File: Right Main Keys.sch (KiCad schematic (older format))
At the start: 6 parts

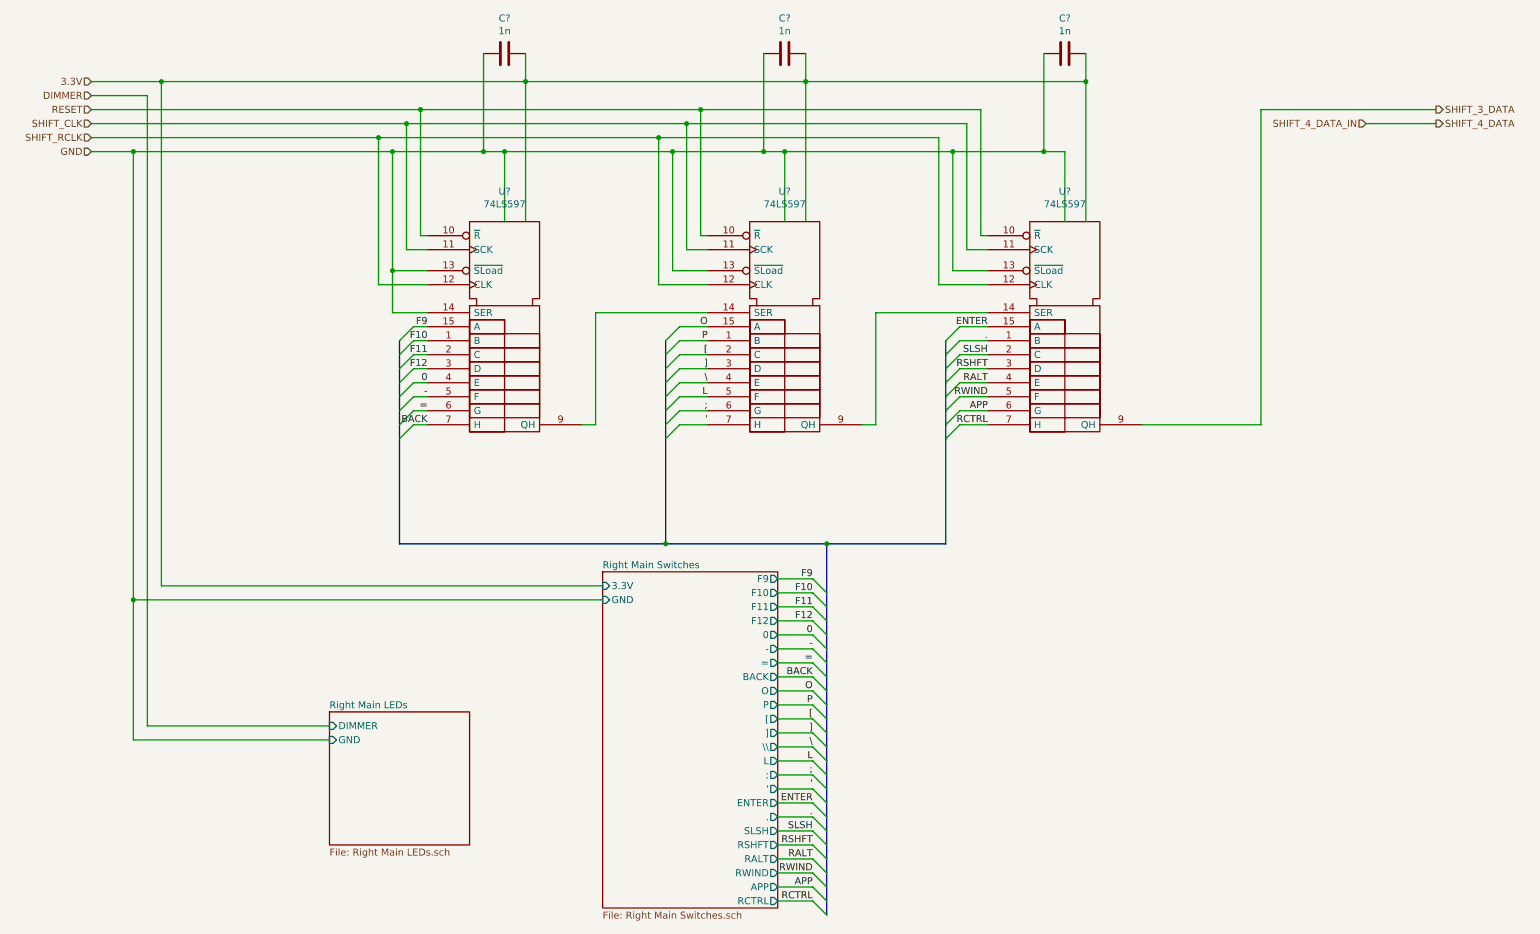
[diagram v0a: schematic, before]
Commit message: Fixed PISO Shift Register Wiring
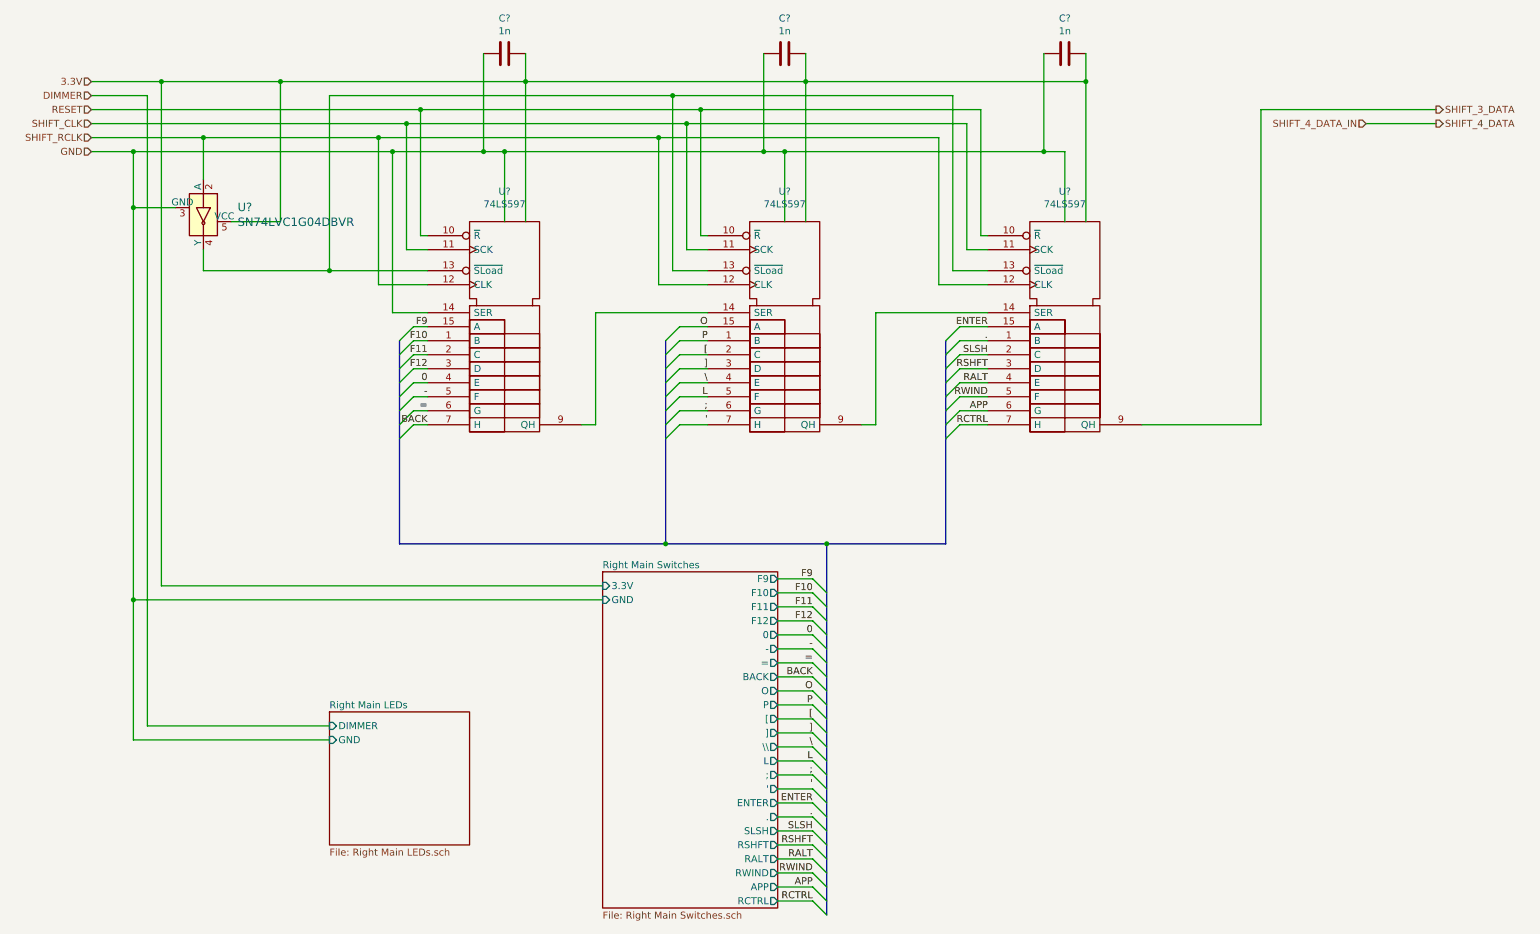
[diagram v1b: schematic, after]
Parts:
- added U?: SN74LVC1G04DBVR, digikey-footprints:SOT-753, symbol dk_Logic-Gates-and-Inverters:SN74LVC1G04DBVR
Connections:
- net GND: now also U?.3 (GND); no longer U?.13 (~SLoad), U?.13 (~SLoad), U?.13 (~SLoad)
- net SHIFT_RCLK: now also U?.2 (A)
- net VCC: now also U?.5 (VCC)
- new net: U?.13 (~SLoad), U?.13 (~SLoad), U?.13 (~SLoad), U?.4 (Y)
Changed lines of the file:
@@
 	3950 1600 3950 2100
-Wire Wire Line
-	3950 1600 5150 1600
 Wire Wire Line
 	5950 1600 5950 2100
@@
 Connection ~ 8100 1100
 Wire Wire Line
-	5950 1600 7150 1600
-Wire Wire Line
 	3350 1300 3350 2200
 Wire Wire Line
@@
 	7250 2300 7400 2300
 Connection ~ 5250 1400
-Wire Wire Line
-	3400 2450 3150 2450
-Wire Wire Line
-	3150 2450 3150 1600
 Connection ~ 3150 1600
 Wire Wire Line
@@
 Connection ~ 3050 1500
 Wire Wire Line
-	5400 2450 5150 2450
-Wire Wire Line
-	5150 2450 5150 1600
-Connection ~ 5150 1600
-Wire Wire Line
-	5150 1600 5800 1600
-Wire Wire Line
-	7400 2450 7150 2450
-Wire Wire Line
-	7150 2450 7150 1600
-Connection ~ 7150 1600
-Wire Wire Line
-	7150 1600 7800 1600
-Wire Wire Line
 	3050 1500 5050 1500
 Wire Wire Line
@@
 	5050 1500 7050 1500
 Wire Wire Line
-	3150 2450 3150 2750
-Wire Wire Line
 	3150 2750 3400 2750
-Connection ~ 3150 2450
 $Comp
 L Device:C C?
@@
 	9350 1300 9350 3550
 Wire Wire Line
-	1500 1100 4100 1100
+	1500 1100 2350 1100
 Connection ~ 1500 1100
 Wire Wire Line
@@
 	1000 1400 3250 1400
 Wire Wire Line
-	1000 1500 3050 1500
+	1000 1500 1800 1500
 Wire Wire Line
 	1300 1600 3150 1600
@@
 	8500 3550 9350 3550
 Wire Wire Line
-	1300 1600 1300 4800
+	1300 1600 1300 2000
 Wire Wire Line
 	4650 4800 1300 4800
@@
 	7100 4400 6250 4400
 Connection ~ 6250 4400
-Wire Bus Line
-	3200 2950 3200 4400
-Wire Bus Line
-	5100 2950 5100 4400
-Wire Bus Line
-	7100 2950 7100 4400
-Wire Bus Line
-	6250 4400 6250 7050
 $Sheet
 S 2700 5600 1000 950
@@
 F3 "GND" I L 2700 5800 50
 $EndSheet
+Wire Wire Line
+	3150 1600 3150 2750
+Wire Wire Line
+	3950 1600 5800 1600
+Wire Wire Line
+	5950 1600 7800 1600
+$Comp
+L dk_Logic-Gates-and-Inverters:SN74LVC1G04DBVR U?
+U 1 1 5EE3072F
+P 1800 2100
+AR Path="/5E8C755A/5EE3072F" Ref="U?"  Part="1"
+AR Path="/5E8C77AE/5EE3072F" Ref="U?"  Part="1"
+F 0 "U?" V 1697 2344 60  0000 L CNN
+F 1 "SN74LVC1G04DBVR" V 1803 2344 60  0000 L CNN
+F 2 "digikey-footprints:SOT-753" H 2000 2300 60  0001 L CNN
+F 3 "http://www.ti.com/general/docs/suppproductinfo.tsp?distId=10&gotoUrl=http%3A%2F%2Fwww.ti.com%2Flit%2Fgpn%2Fsn74lvc1g04" H 2000 2400 60  0001 L CNN
+F 4 "296-11599-1-ND" H 2000 2500 60  0001 L CNN "Digi-Key_PN"
+F 5 "SN74LVC1G04DBVR" H 2000 2600 60  0001 L CNN "MPN"
+F 6 "Integrated Circuits (ICs)" H 2000 2700 60  0001 L CNN "Category"
+F 7 "Logic - Gates and Inverters" H 2000 2800 60  0001 L CNN "Family"
+F 8 "http://www.ti.com/general/docs/suppproductinfo.tsp?distId=10&gotoUrl=http%3A%2F%2Fwww.ti.com%2Flit%2Fgpn%2Fsn74lvc1g04" H 2000 2900 60  0001 L CNN "DK_Datasheet_Link"
+F 9 "/product-detail/en/texas-instruments/SN74LVC1G04DBVR/296-11599-1-ND/385738" H 2000 3000 60  0001 L CNN "DK_Detail_Page"
+F 10 "IC INVERTER 1CH 1-INP SOT23-5" H 2000 3100 60  0001 L CNN "Description"
+F 11 "Texas Instruments" H 2000 3200 60  0001 L CNN "Manufacturer"
+F 12 "Active" H 2000 3300 60  0001 L CNN "Status"
+	1    1800 2100
+	0    1    1    0
+$EndComp
+Wire Wire Line
+	1800 1800 1800 1500
+Connection ~ 1800 1500
+Wire Wire Line
+	1800 1500 3050 1500
+Wire Wire Line
+	1600 2000 1300 2000
+Connection ~ 1300 2000
+Wire Wire Line
+	1300 2000 1300 4800
+Wire Wire Line
+	2000 2100 2350 2100
+Wire Wire Line
+	2350 2100 2350 1100
+Connection ~ 2350 1100
+Wire Wire Line
+	2350 1100 4100 1100
+Wire Wire Line
+	1800 2300 1800 2450
+Wire Wire Line
+	1800 2450 2700 2450
+Wire Wire Line
+	2700 2450 2700 1200
+Wire Wire Line
+	2700 1200 5150 1200
+Wire Wire Line
+	5150 1200 5150 2450
+Wire Wire Line
+	5150 2450 5400 2450
+Connection ~ 2700 2450
+Wire Wire Line
+	2700 2450 3400 2450
+Wire Wire Line
+	5150 1200 7150 1200
+Wire Wire Line
+	7150 1200 7150 2450
+Wire Wire Line
+	7150 2450 7400 2450
+Connection ~ 5150 1200
+Wire Bus Line
+	3200 2950 3200 4400
+Wire Bus Line
+	5100 2950 5100 4400
+Wire Bus Line
+	7100 2950 7100 4400
+Wire Bus Line
+	6250 4400 6250 7050
 $EndSCHEMATC

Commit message: Corrected errors found in design rule check
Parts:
- C61, C62, C63: renamed from C?; footprint (none) -> Capacitor_SMD:C_1206_3216Metric_Pad1.42x1.75mm_HandSolder
- U13, U14, U15: renamed from U?; footprint (none) -> Package_SO:SOIC-16_3.9x9.9mm_P1.27mm
- gave numbers to parts that had none: 1
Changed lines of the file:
@@
 SHIFT_3_DATA
 $Comp
-L 74xx_IEEE:74LS597 U?
+L 74xx_IEEE:74LS597 U13
 U 1 1 5F4969E5
 P 3950 2900
-AR Path="/5E8C77AE/5F4969E5" Ref="U?"  Part="1"
+AR Path="/5E8C77AE/5F4969E5" Ref="U13"  Part="1"
 AR Path="/5E8C755A/5F4969E5" Ref="U?"  Part="1"
-F 0 "U?" H 3950 3916 50  0000 C CNN
+F 0 "U13" H 3950 3916 50  0000 C CNN
 F 1 "74LS597" H 3950 3825 50  0000 C CNN
-F 2 "" H 3950 2900 50  0001 C CNN
+F 2 "Package_SO:SOIC-16_3.9x9.9mm_P1.27mm" H 3950 2900 50  0001 C CNN
 F 3 "" H 3950 2900 50  0001 C CNN
 	1    3950 2900
@@
 $EndComp
 $Comp
-L 74xx_IEEE:74LS597 U?
+L 74xx_IEEE:74LS597 U14
 U 1 1 5F4969EB
 P 5950 2900
-AR Path="/5E8C77AE/5F4969EB" Ref="U?"  Part="1"
+AR Path="/5E8C77AE/5F4969EB" Ref="U14"  Part="1"
 AR Path="/5E8C755A/5F4969EB" Ref="U?"  Part="1"
-F 0 "U?" H 5950 3916 50  0000 C CNN
+F 0 "U14" H 5950 3916 50  0000 C CNN
 F 1 "74LS597" H 5950 3825 50  0000 C CNN
-F 2 "" H 5950 2900 50  0001 C CNN
+F 2 "Package_SO:SOIC-16_3.9x9.9mm_P1.27mm" H 5950 2900 50  0001 C CNN
 F 3 "" H 5950 2900 50  0001 C CNN
 	1    5950 2900
@@
 $EndComp
 $Comp
-L 74xx_IEEE:74LS597 U?
+L 74xx_IEEE:74LS597 U15
 U 1 1 5F4969F1
 P 7950 2900
-AR Path="/5E8C77AE/5F4969F1" Ref="U?"  Part="1"
+AR Path="/5E8C77AE/5F4969F1" Ref="U15"  Part="1"
 AR Path="/5E8C755A/5F4969F1" Ref="U?"  Part="1"
-F 0 "U?" H 7950 3916 50  0000 C CNN
+F 0 "U15" H 7950 3916 50  0000 C CNN
 F 1 "74LS597" H 7950 3825 50  0000 C CNN
-F 2 "" H 7950 2900 50  0001 C CNN
+F 2 "Package_SO:SOIC-16_3.9x9.9mm_P1.27mm" H 7950 2900 50  0001 C CNN
 F 3 "" H 7950 2900 50  0001 C CNN
 	1    7950 2900
@@
 Wire Wire Line
 	4100 1100 6100 1100
-Wire Wire Line
-	6100 1100 6100 2100
 Connection ~ 4100 1100
 Wire Wire Line
@@
 	3150 2750 3400 2750
 $Comp
-L Device:C C?
+L Device:C C61
 U 1 1 5F496A39
 P 3950 900
-AR Path="/5E8C77AE/5F496A39" Ref="C?"  Part="1"
+AR Path="/5E8C77AE/5F496A39" Ref="C61"  Part="1"
 AR Path="/5E8C755A/5F496A39" Ref="C?"  Part="1"
-F 0 "C?" V 3698 900 50  0000 C CNN
+F 0 "C61" V 3698 900 50  0000 C CNN
 F 1 "1n" V 3789 900 50  0000 C CNN
-F 2 "" H 3988 750 50  0001 C CNN
+F 2 "Capacitor_SMD:C_1206_3216Metric_Pad1.42x1.75mm_HandSolder" H 3988 750 50  0001 C CNN
 F 3 "~" H 3950 900 50  0001 C CNN
 	1    3950 900
@@
 $EndComp
 $Comp
-L Device:C C?
+L Device:C C62
 U 1 1 5F496A3F
 P 5950 900
-AR Path="/5E8C77AE/5F496A3F" Ref="C?"  Part="1"
+AR Path="/5E8C77AE/5F496A3F" Ref="C62"  Part="1"
 AR Path="/5E8C755A/5F496A3F" Ref="C?"  Part="1"
-F 0 "C?" V 5698 900 50  0000 C CNN
+F 0 "C62" V 5698 900 50  0000 C CNN
 F 1 "1n" V 5789 900 50  0000 C CNN
-F 2 "" H 5988 750 50  0001 C CNN
+F 2 "Capacitor_SMD:C_1206_3216Metric_Pad1.42x1.75mm_HandSolder" H 5988 750 50  0001 C CNN
 F 3 "~" H 5950 900 50  0001 C CNN
 	1    5950 900
@@
 $EndComp
 $Comp
-L Device:C C?
+L Device:C C63
 U 1 1 5F496A45
 P 7950 900
-AR Path="/5E8C77AE/5F496A45" Ref="C?"  Part="1"
+AR Path="/5E8C77AE/5F496A45" Ref="C63"  Part="1"
 AR Path="/5E8C755A/5F496A45" Ref="C?"  Part="1"
-F 0 "C?" V 7698 900 50  0000 C CNN
+F 0 "C63" V 7698 900 50  0000 C CNN
 F 1 "1n" V 7789 900 50  0000 C CNN
-F 2 "" H 7988 750 50  0001 C CNN
+F 2 "Capacitor_SMD:C_1206_3216Metric_Pad1.42x1.75mm_HandSolder" H 7988 750 50  0001 C CNN
 F 3 "~" H 7950 900 50  0001 C CNN
 	1    7950 900
@@
 Wire Wire Line
 	3800 1600 3950 1600
-Wire Wire Line
-	6100 1100 6100 900
 Wire Wire Line
 	5800 900  5800 1600
@@
 P 1800 2100
 AR Path="/5E8C755A/5EE3072F" Ref="U?"  Part="1"
-AR Path="/5E8C77AE/5EE3072F" Ref="U?"  Part="1"
-F 0 "U?" V 1697 2344 60  0000 L CNN
+AR Path="/5E8C77AE/5EE3072F" Ref="U12"  Part="1"
+F 0 "U12" V 1697 2344 60  0000 L CNN
 F 1 "SN74LVC1G04DBVR" V 1803 2344 60  0000 L CNN
 F 2 "digikey-footprints:SOT-753" H 2000 2300 60  0001 L CNN
@@
 	7150 2450 7400 2450
 Connection ~ 5150 1200
+Wire Wire Line
+	6100 1100 6100 900
+Wire Wire Line
+	6100 1100 6100 2100
+Wire Bus Line
+	7100 2950 7100 4400
+Wire Bus Line
+	5100 2950 5100 4400
 Wire Bus Line
 	3200 2950 3200 4400
 Wire Bus Line
-	5100 2950 5100 4400
-Wire Bus Line
-	7100 2950 7100 4400
-Wire Bus Line
 	6250 4400 6250 7050
